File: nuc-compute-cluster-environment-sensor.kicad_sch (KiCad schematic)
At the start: 23 parts

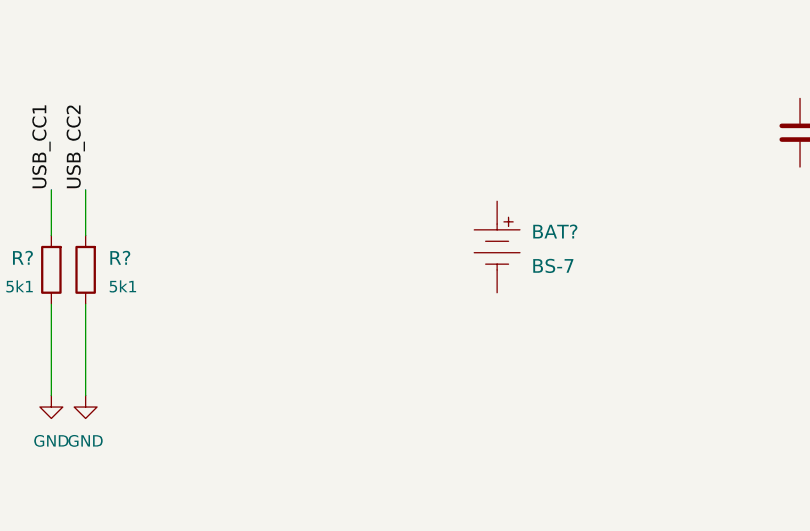
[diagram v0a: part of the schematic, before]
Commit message: [#39832] SCH: Change battery holder to CR1216/CR1225 STM one
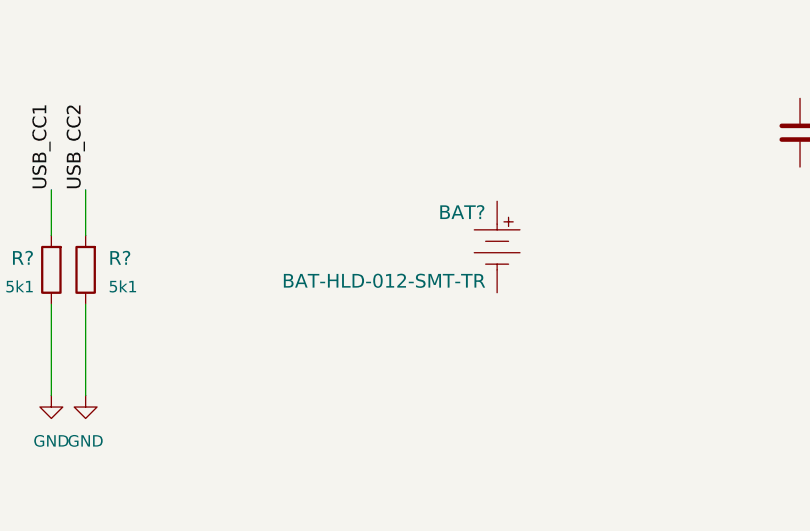
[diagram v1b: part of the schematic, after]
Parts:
- BAT?: value BS-7 -> BAT-HLD-012-SMT-TR; footprint antmicro-footprints:Battery_Holder_Coin_2032_BS-7 -> antmicro-footprints:BAT_BAT-HLD-012-SMT-TR; symbol antmicroBatteryHoldersClipsContacts:BS-7 -> antmicroBatteryHoldersClipsContacts:BAT-HLD-012-SMT-TR; License (none) -> Copyright (c) 2022 Antmicro <www.antmicro.com> [Apache2 lic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; MPN BS-7 -> BAT-HLD-012-SMT-TR; Manufacturer MPD (Memory Protection Devices) -> Linx Technologies
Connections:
- new net: BAT?.P1, BAT?.P2

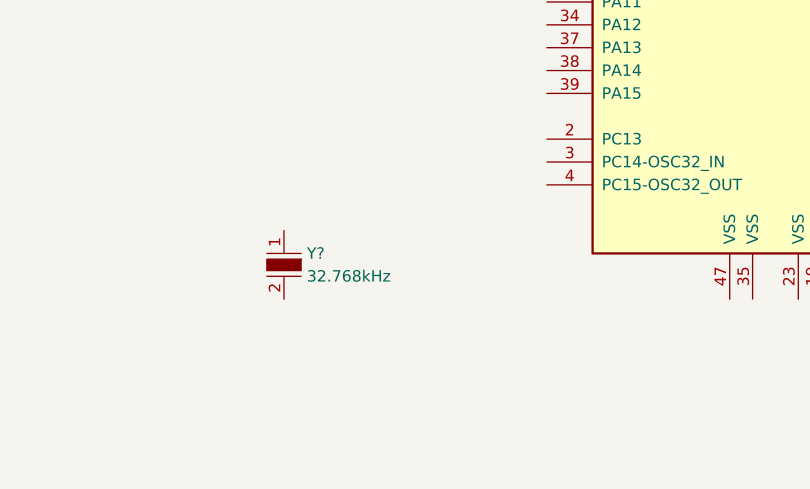
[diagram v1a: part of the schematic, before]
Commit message: [#39832] SCH: Wire up 32kHz RTC crystal to MCU
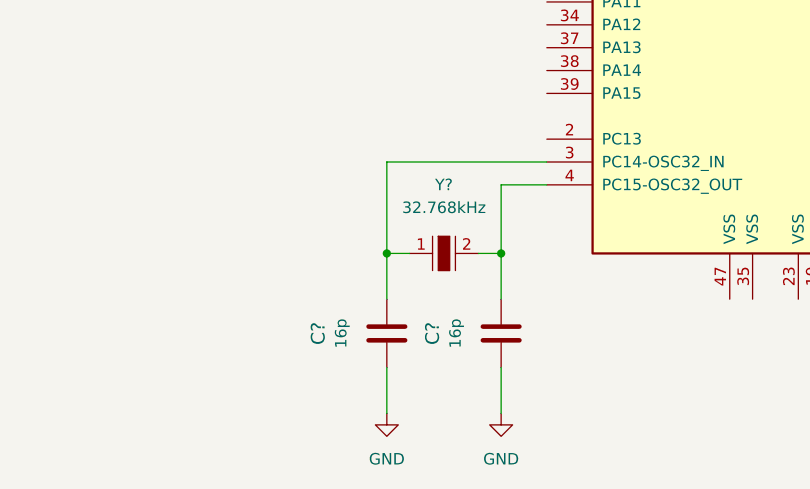
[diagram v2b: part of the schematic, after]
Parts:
- added C? (x2): C_16p_0402, antmicro-footprints:0402-res, symbol antmicroCapacitors0402:C_16p_0402
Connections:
- net GND: now also C?.1, C?.1
- net at U?.3 (PC14-OSC32_IN): now also Y?.1, C?.2
- net at U?.4 (PC15-OSC32_OUT): now also Y?.2, C?.2
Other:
- moved on the sheet: Y?

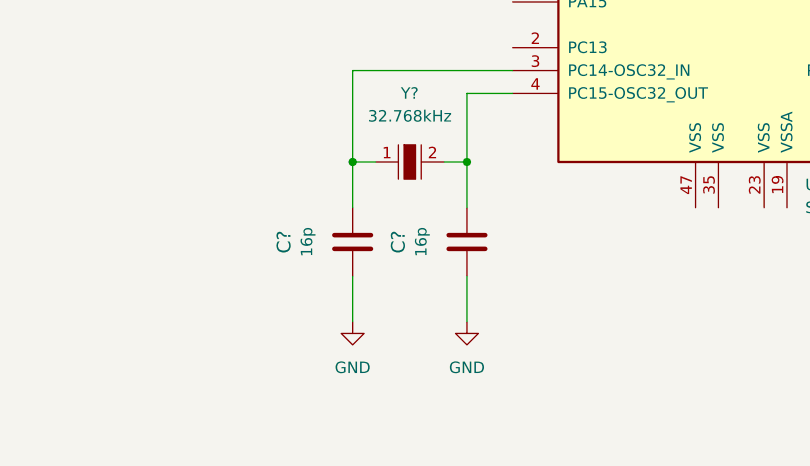
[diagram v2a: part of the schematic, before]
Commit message: [#39832] SCH: Add an DNP parallel 1M resistor to 32kHz RTC crystal for eventual oscillation stabilization
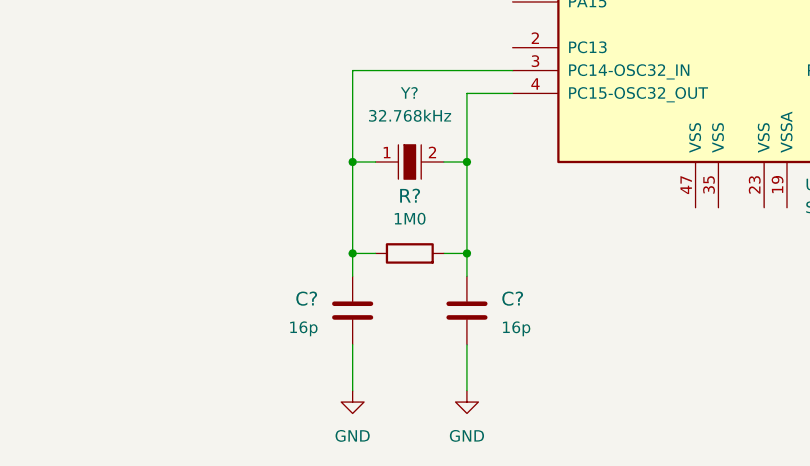
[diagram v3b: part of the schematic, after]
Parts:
- added R?: R_1M0_0402, antmicro-footprints:0402-res, symbol antmicroResistors0402:R_1M0_0402
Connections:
- net at C?.2, U?.3 (PC14-OSC32_IN), Y?.1: now also R?.1
- net at C?.2, U?.4 (PC15-OSC32_OUT), Y?.2: now also R?.2
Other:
- moved on the sheet: C?

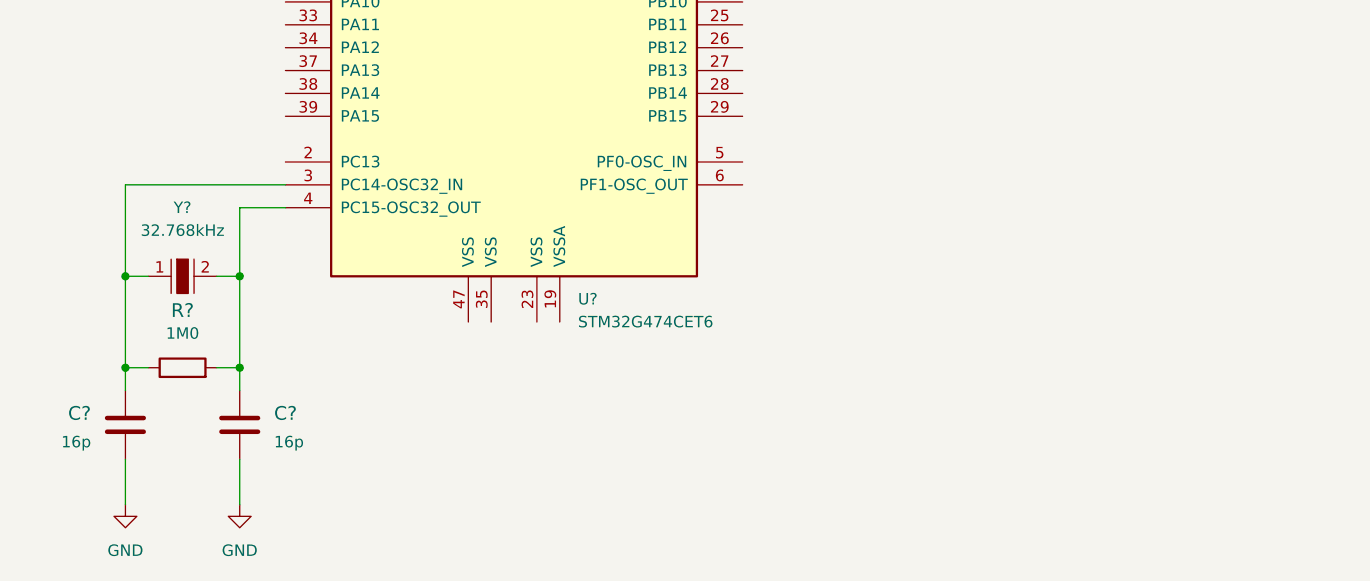
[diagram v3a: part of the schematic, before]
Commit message: [#39832] SCH: Add & wire up 8MH main MCU ceramic oscillator
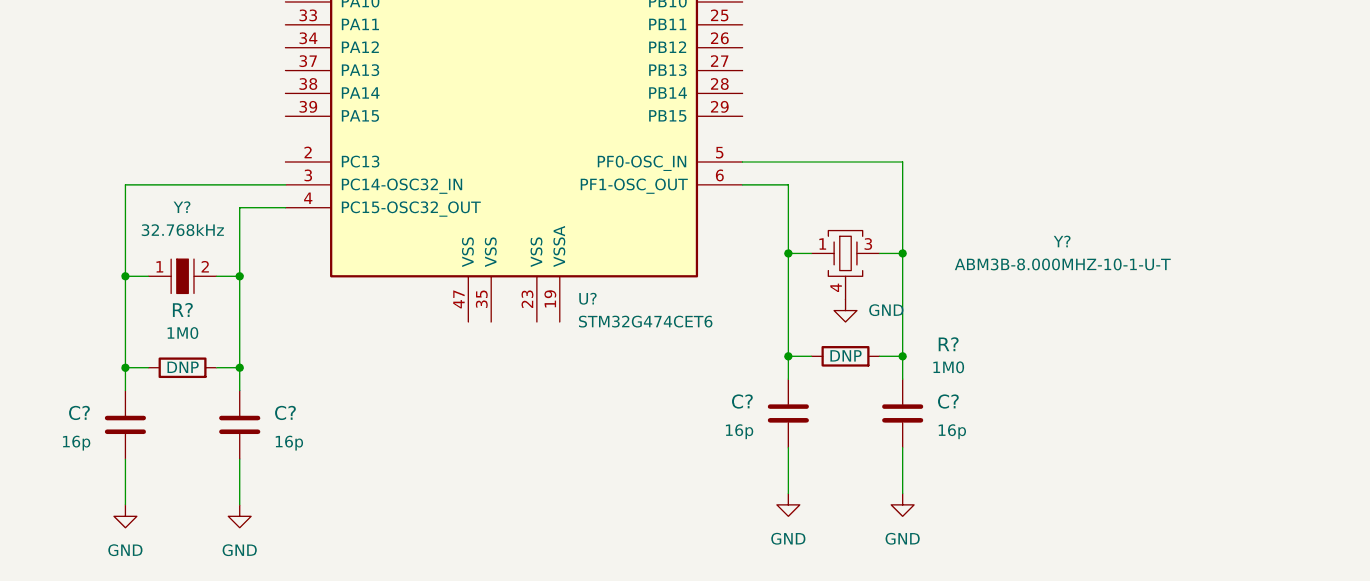
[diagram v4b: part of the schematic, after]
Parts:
- added C? (x2): C_16p_0402, antmicro-footprints:0402-res, symbol antmicroCapacitors0402:C_16p_0402
- added R?: R_1M0_0402, antmicro-footprints:0402-res, symbol antmicroResistors0402:R_1M0_0402
- added Y?: ABM3B-8.000MHZ-10-1-U-T, antmicro-footprints:ABM3B, symbol antmicroCrystals:ABM3B-8.000MHZ-10-1-U-T
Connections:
- net GND: now also C?.1, C?.1, Y?.2, Y?.4
- net at U?.5 (PF0-OSC_IN): now also C?.2, R?.2, Y?.3
- net at U?.6 (PF1-OSC_OUT): now also C?.2, R?.1, Y?.1

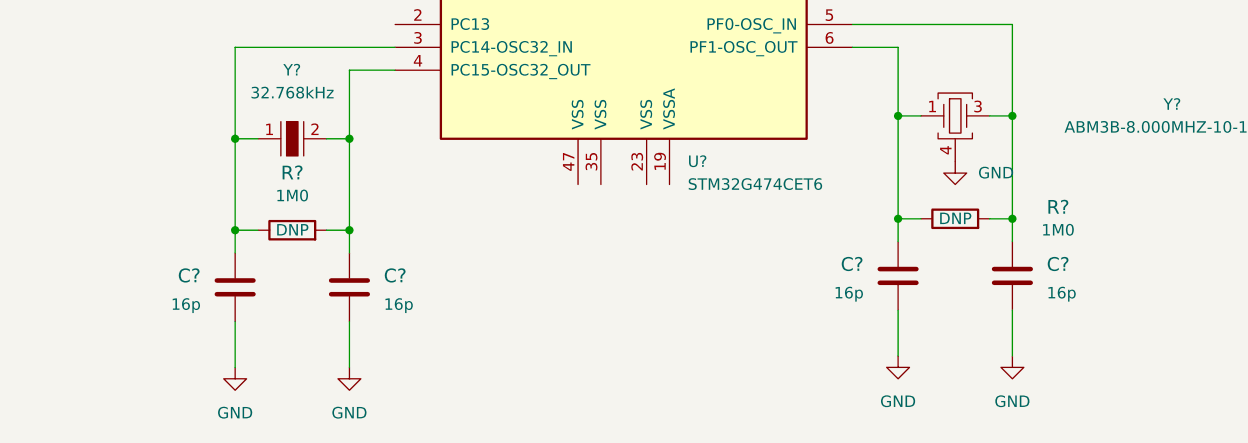
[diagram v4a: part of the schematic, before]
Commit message: [#39832] SCH: Adjust 8MHz oscillator load capacitors
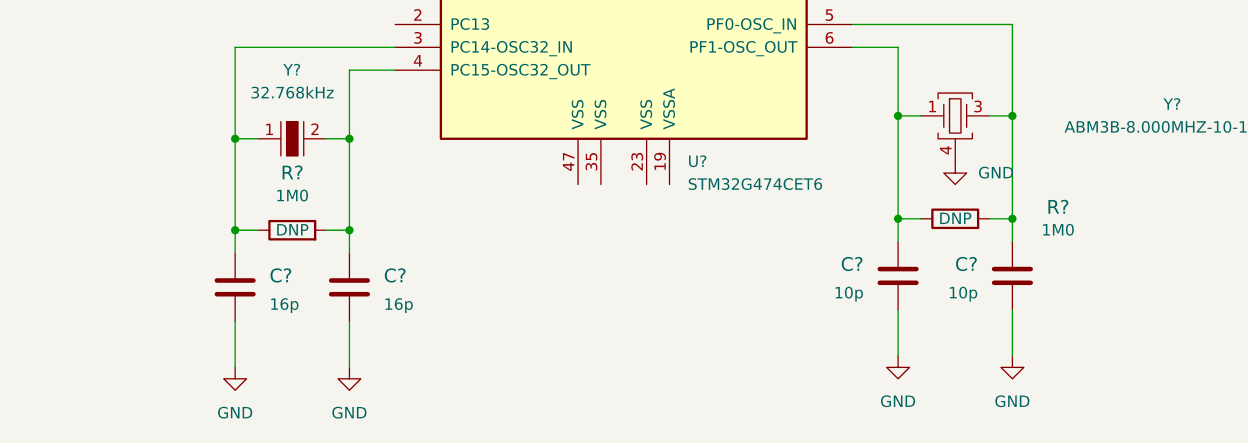
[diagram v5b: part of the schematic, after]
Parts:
- C? (x2): value C_16p_0402 -> C_10p_0402; footprint antmicro-footprints:0402-res -> antmicro-footprints:0402-cap; symbol antmicroCapacitors0402:C_16p_0402 -> antmicroCapacitors0402:C_10p_0402; MPN 0402N160J500CT -> MC0402N100D500CT; Manufacturer Walsin -> MULTICOMP; Val 16p -> 10p

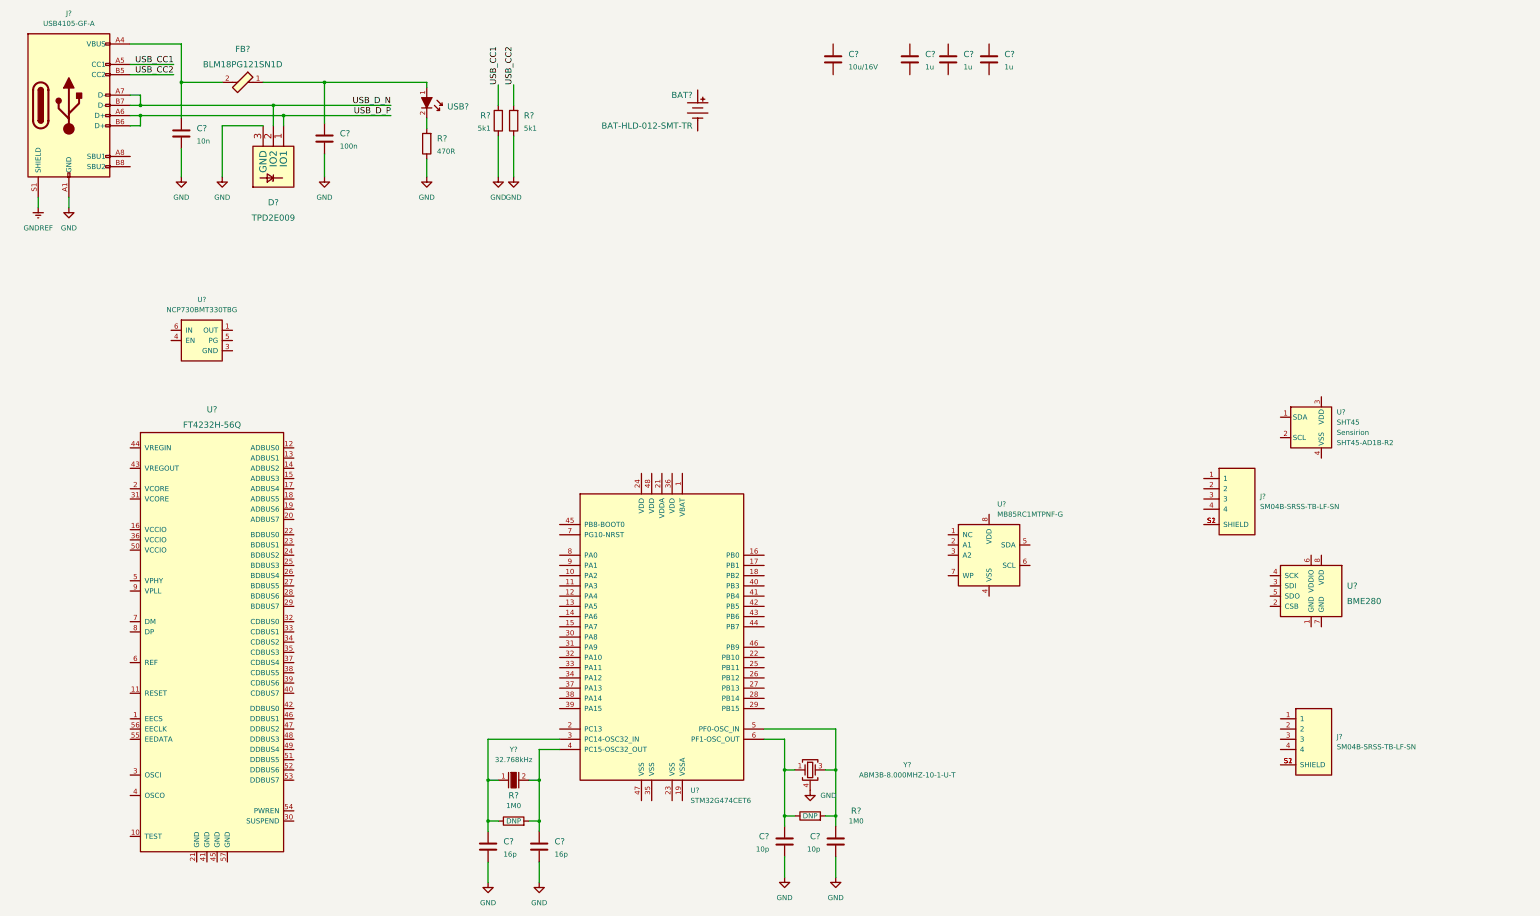
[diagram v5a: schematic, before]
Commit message: [#39832] SCH: Complete circuitry near USB-C & 3V3 LDO, connect BAT to MCU
Complete changelog:
- Connect battery to MCU,
- add more ESD protection to USB-C,
- rearrange schematic,
- increase filtering caps on USB-C input to 2x2u2,
- change caps to 0402 where possible,
- wire up dedicated 3V3 LDO.
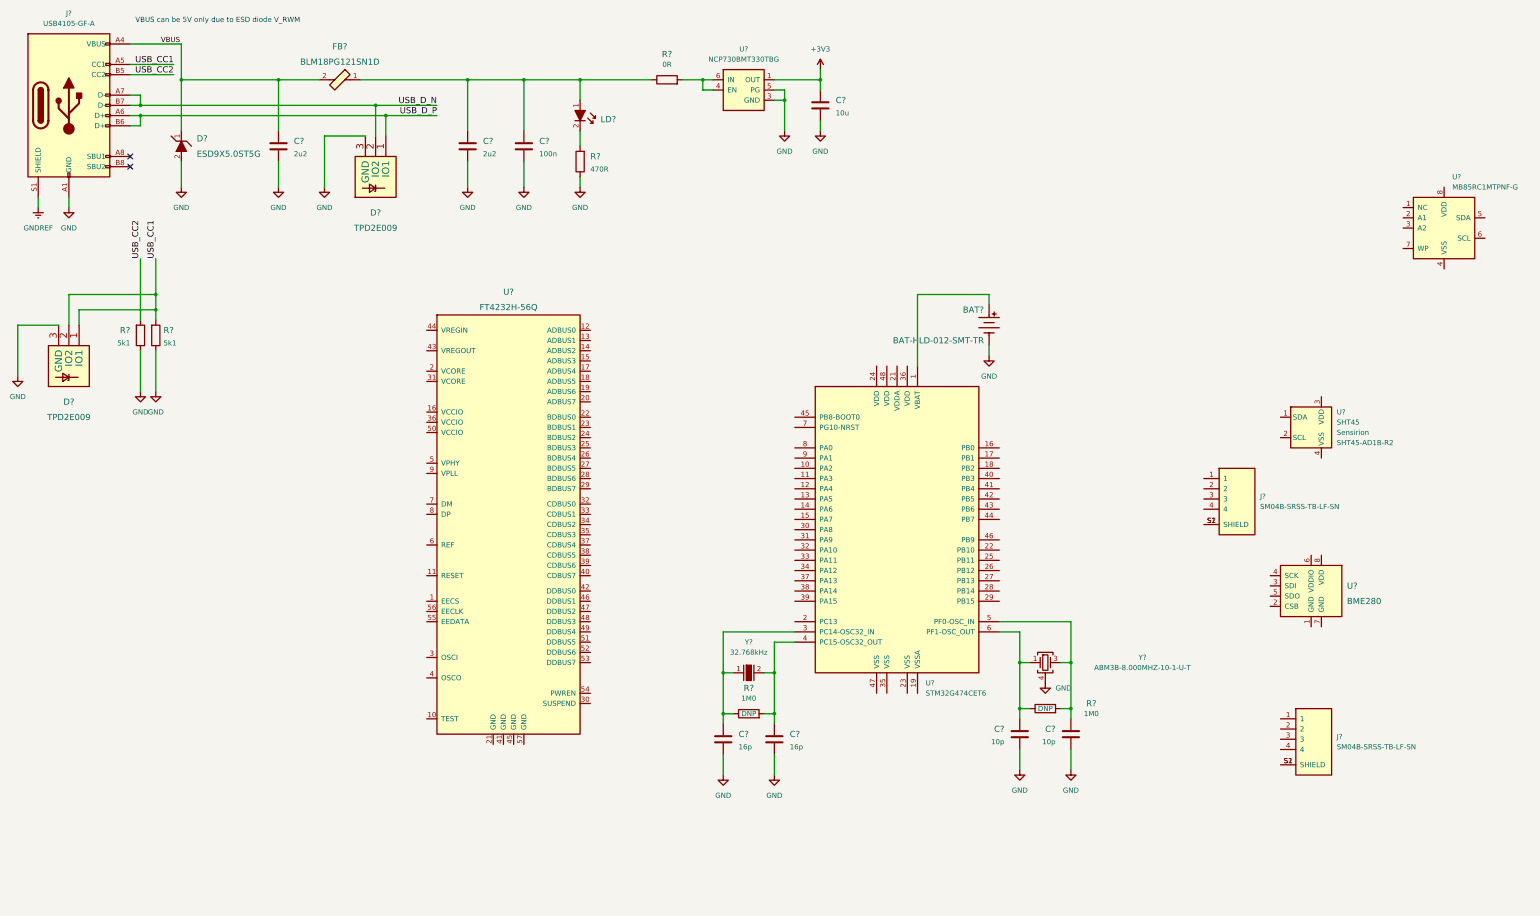
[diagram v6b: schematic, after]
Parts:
- removed C?: C_100n_0402_16V, antmicro-footprints:0603-cap, symbol antmicroCapacitors0603:C_100n_0603
- removed C? (x3): C_1u_0603, antmicro-footprints:0603-cap, symbol antmicroCapacitors0603:C_1u_0603
- removed C?: C_10n_0402, antmicro-footprints:0603-cap, symbol antmicroCapacitors0603:C_10n_0603
- removed C?: C_10u_16V_0603, antmicro-footprints:0603-cap, symbol antmicroCapacitors0603:C_10u_16V_0603
- added C? (x2): C_2u2_0402, antmicro-footprints:0402-cap, symbol antmicroCapacitors0402:C_2u2_0402
- added C?: C_100n_0402, antmicro-footprints:0402-cap, symbol antmicroCapacitors0402:C_100n_0402
- added C?: C_10u_0402, antmicro-footprints:0402-cap, symbol antmicroCapacitors0402:C_10u_0402
- added D?: ESD9X5.0ST5G, antmicro-footprints:SOD-923, symbol antmicroTVSDiodes:ESD9X5.0ST5G
- added D?: TPD2E009, antmicro-footprints:SOT-723, symbol antmicroTVSDiodes:TPD2E009
- added R?: R_0R_0402, antmicro-footprints:0402-res, symbol antmicroResistors0402:R_0R_0402
- R?: footprint antmicro-footprints:0603-res -> antmicro-footprints:0402-res; symbol antmicroResistors0603:R_470R_0603 -> antmicroResistors0402:R_470R_0402; MPN CR0603-JW-471GLF -> CRCW0402470RFKED; Manufacturer BOURNS -> VISHAY
- gave numbers to parts that had none: 1
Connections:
- net GND: now also BAT?.N, U?.3 (GND), U?.5 (PG), U?.7 (EP), C?.2, C?.2, C?.2, C?.2, D?.2, D?.3 (GND)
- net USB_CC1: now also D?.1 (IO1), D?.2 (IO2)
- net +3V3: now reaches U?.1 (OUT)
- net +3V3: now also C?.1
- net at U?.4 (EN): now also U?.6 (IN), R?.2
- net at FB?.1, LD?.1: now also C?.1, C?.1, R?.1
- net at U?.1 (VBAT): now also BAT?.P1, BAT?.P2
- net VBUS: now reaches FB?.2, J?.A4 (VBUS), J?.A9 (VBUS), J?.B4 (VBUS), J?.B9 (VBUS)
- net VBUS: now also C?.1, D?.1
- no-connect marks 0 -> 2
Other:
- note added: "VBUS can be 5V only due to ESD diode V_RWM"
- moved on the sheet: BAT?, C?, D?, FB?, LD?, R?, U?, Y?
